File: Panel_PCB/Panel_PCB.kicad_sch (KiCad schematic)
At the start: 87 parts, among them J1 DC, J10 Relay 3, J11 Relay 4, J12 Terminal A, J13 Terminal B, J14 Boton D (4), J2 Bateria, J3 Sensor IN, J4 Sensor OUT, J5 Boton A (1), J6 Boton B (2), J7 Boton C (3), J8 Relay 1, J9 Relay 2, K1 SANYOU_SRD_Form_C, K2 SANYOU_SRD_Form_C, K3 SANYOU_SRD_Form_C, K4 SANYOU_SRD_Form_C, K5 EC2-4.5SNU, K7 SANYOU_SRD_Form_C, Q1 2N2222A, Q2 2N2222A, Q3 2N2222A, Q4 2N2222A, Q7 2N2222A, U1 TLP291, U10 LM1117T-3.3, U12 DS1307+, U13 LM311, U2 TLP291, U3 TLP291, U4 TLP291, U5 LM7805_TO220, U6 LM1117T-3.3, U7 LM7805_TO220, U8 LM7805_TO220, U9 LM1117T-3.3, Y1 Crystal

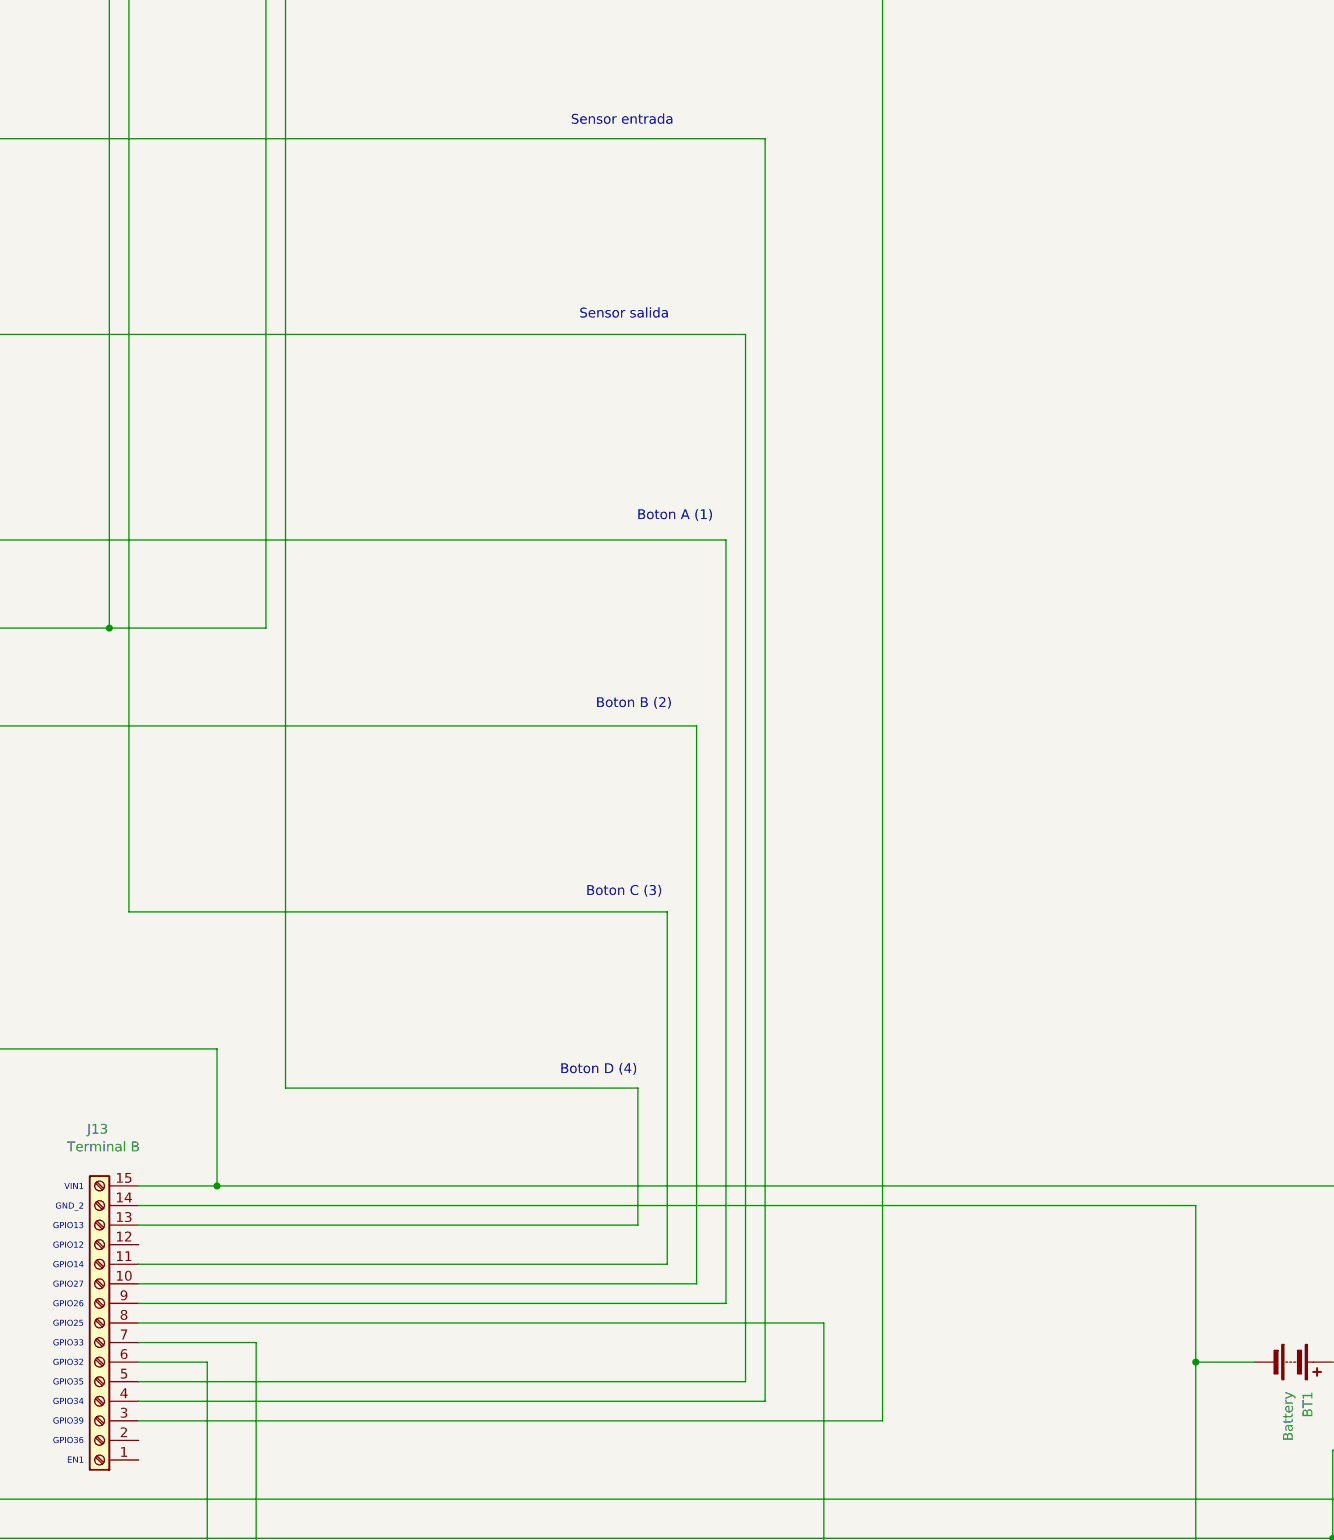
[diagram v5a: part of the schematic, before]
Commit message: Actualización de esquematico: resistencias de pulldown a los pines de los sensores
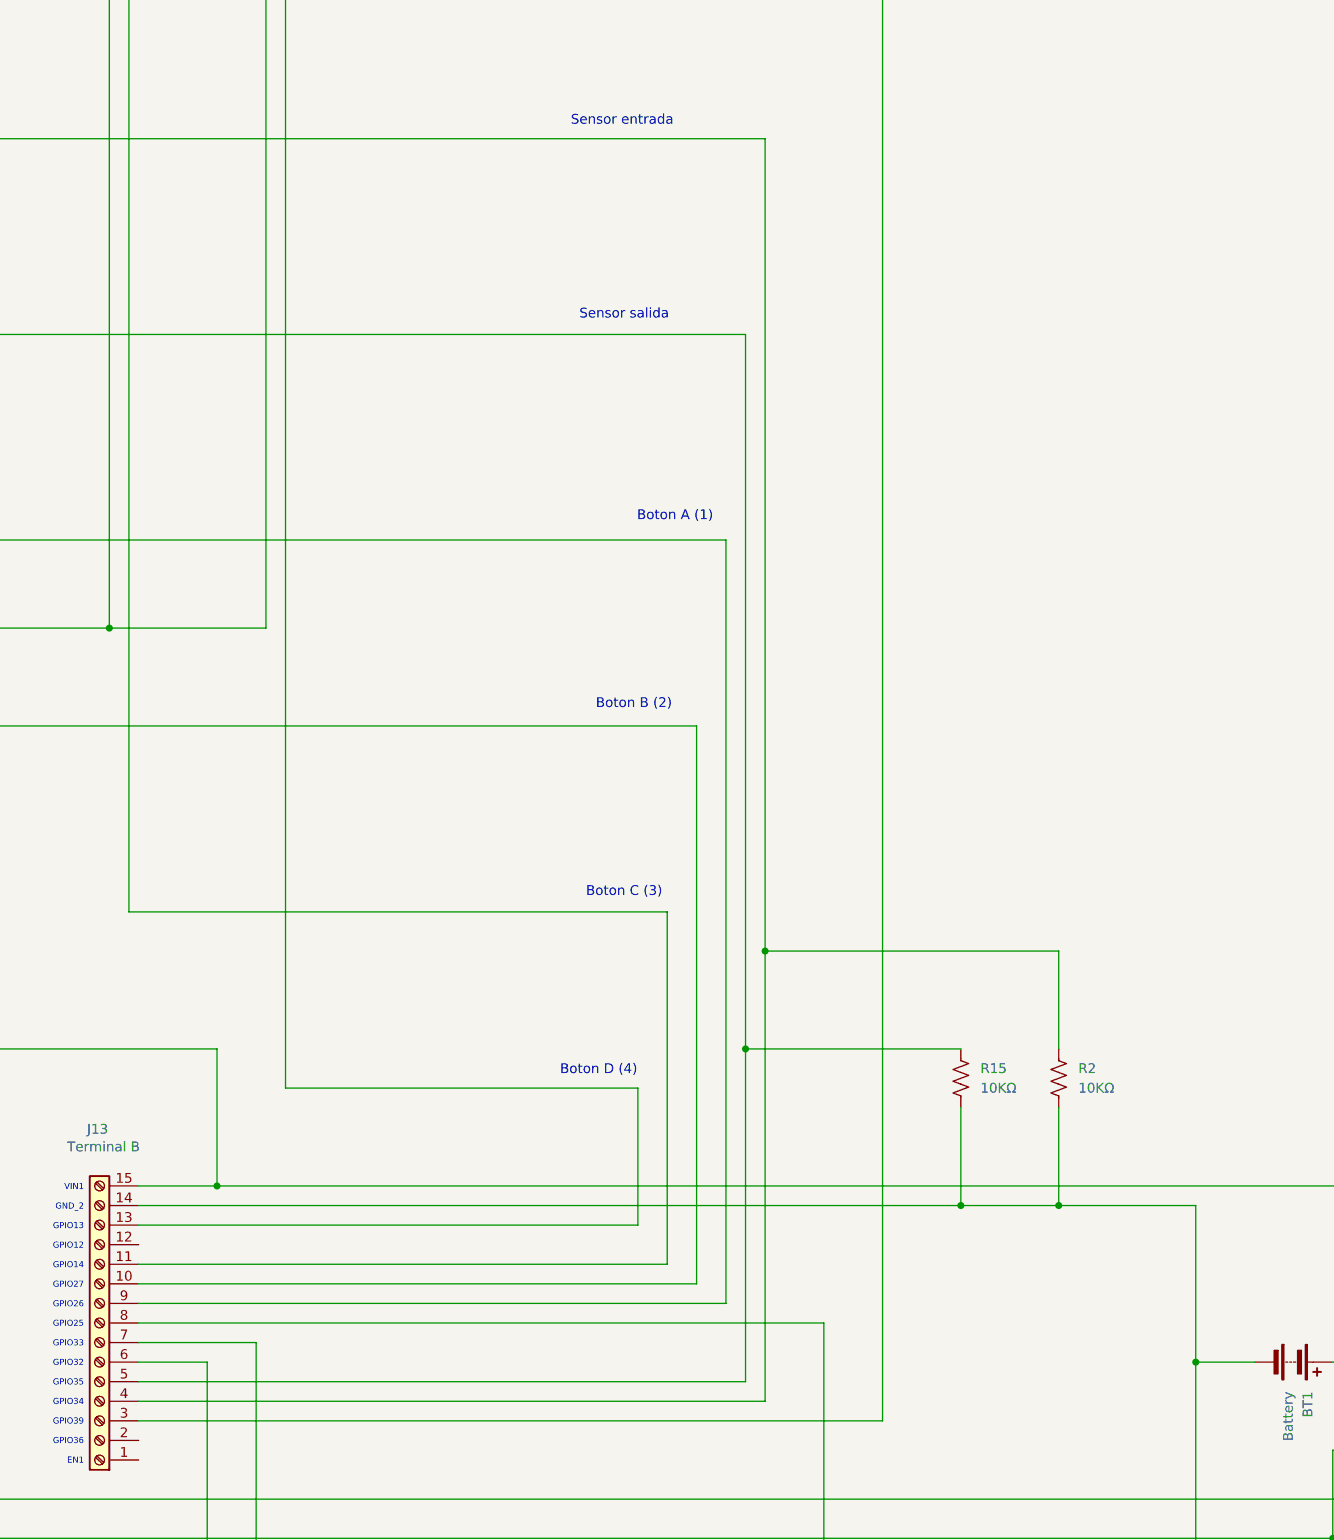
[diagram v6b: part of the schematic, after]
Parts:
- added R15, R2: 10KΩ, Resistor_THT:R_Axial_DIN0207_L6.3mm_D2.5mm_P10.16mm_Horizontal, symbol Device:R_US
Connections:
- net at J13.4 (Pin_4), J3.2 (Pin_2): now also R2.1
- net at J13.5 (Pin_5), J4.2 (Pin_2): now also R15.1
- net at BT1.2 (-), J13.14 (Pin_14), U12.4 (GND): now also R15.2, R2.2

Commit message: Actualización de esquematico
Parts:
- removed D18: 1N4001, Diode_THT:D_DO-41_SOD81_P10.16mm_Horizontal, symbol Diode:1N4001
- removed D2: 12 V, Diode_THT:D_DO-41_SOD81_P10.16mm_Horizontal, symbol Device:D_Zener
- added C4, C5: 25V 4700μF, Capacitor_THT:C_Radial_D18.0mm_H35.5mm_P7.50mm, symbol Device:C_US
- C2: value 35V 4700μF -> 25V 4700μF
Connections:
- net at C10.2, C11.2, C12.2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: now also C4.2, C5.2
- net at C2.1, C7.1, C9.1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: now also C4.1, C5.1
- net at J2.1 (Pin_1), K5.10, K7.3: now also U13.2 (+)
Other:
- note added: "Crear un log de 1 byte para guardar los estados de las salidad (considerar si se necesitan guardar los estados de las entradas)"
- moved on the sheet: C2

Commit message: Información para usar el control remoto
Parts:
- added C6: 25V 4700μF, Capacitor_THT:C_Radial_D18.0mm_H35.5mm_P7.50mm, symbol Device:C_US
- added J15: Control remoto, TerminalBlock:TerminalBlock_Xinya_XY308-2.54-7P_1x07_P2.54mm_Horizontal, symbol Connector:Screw_Terminal_01x07
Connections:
- net at C10.2, C11.2, C12.2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: now also C6.2
- net at C10.1, J12.11 (Pin_11), J12.14 (Pin_14)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: now also C6.1
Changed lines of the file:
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@@
 	)
 	(junction
+		(at 466.09 247.65)
+		(diameter 0)
+		(color 0 0 0 0)
+	)
+	(junction
 		(at 482.6 50.8)
 		(diameter 0)
@@
 	)
 	(junction
+		(at 466.09 267.97)
+		(diameter 0)
+		(color 0 0 0 0)
+	)
+	(junction
 		(at 175.26 106.68)
 		(diameter 0)
@@
 	(wire
 		(pts
-			(xy 435.61 247.65) (xy 542.29 247.65)
+			(xy 435.61 247.65) (xy 466.09 247.65)
 		)
 		(stroke
@@
 	(wire
 		(pts
-			(xy 435.61 267.97) (xy 499.11 267.97)
+			(xy 435.61 267.97) (xy 466.09 267.97)
 		)
 		(stroke
@@
 	(wire
 		(pts
+			(xy 466.09 261.62) (xy 466.09 267.97)
+		)
+		(stroke
+			(width 0)
+			(type default)
+			(color 0 0 0 1)
+		)
+	)
+	(wire
+		(pts
 			(xy 433.07 238.76) (xy 433.07 193.04)
 		)
@@
 	(wire
 		(pts
+			(xy 466.09 267.97) (xy 499.11 267.97)
+		)
+		(stroke
+			(width 0)
+			(type default)
+			(color 0 0 0 1)
+		)
+	)
+	(wire
+		(pts
 			(xy 509.27 107.95) (xy 509.27 205.74)
 		)
@@
 	(wire
 		(pts
+			(xy 466.09 247.65) (xy 466.09 254)
+		)
+		(stroke
+			(width 0)
+			(type default)
+			(color 255 0 0 1)
+		)
+	)
+	(wire
+		(pts
 			(xy 330.2 173.99) (xy 330.2 176.53)
 		)
@@
 	(wire
 		(pts
+			(xy 466.09 247.65) (xy 542.29 247.65)
+		)
+		(stroke
+			(width 0)
+			(type default)
+			(color 255 0 0 1)
+		)
+	)
+	(wire
+		(pts
 			(xy 398.78 339.09) (xy 414.02 339.09)
 		)
@@
 	)
 	(symbol
+		(lib_id "Device:C_US")
+		(at 466.09 257.81 0)
+		(unit 1)
+		(exclude_from_sim no)
+		(in_bom yes)
+		(on_board yes)
+		(dnp no)
+		(fields_autoplaced yes)
+		(property "Reference" "C6"
+			(at 469.9 256.7939 0)
+			(effects
+				(font
+					(size 1.27 1.27)
+				)
+				(justify left)
+			)
+		)
+		(property "Value" "25V  4700μF"
+			(at 469.9 259.3339 0)
+			(effects
+				(font
+					(size 1.27 1.27)
+				)
+				(justify left)
+			)
+		)
+		(property "Footprint" "Capacitor_THT:C_Radial_D18.0mm_H35.5mm_P7.50mm"
+			(at 466.09 257.81 0)
+			(effects
+				(font
+					(size 1.27 1.27)
+				)
+				(hide yes)
+			)
+		)
+		(property "Datasheet" ""
+			(at 466.09 257.81 0)
+			(effects
+				(font
+					(size 1.27 1.27)
+				)
+				(hide yes)
+			)
+		)
+		(property "Description" "capacitor, US symbol"
+			(at 466.09 257.81 0)
+			(effects
+				(font
+					(size 1.27 1.27)
+				)
+				(hide yes)
+			)
+		)
+		(pin "2"
+		)
+		(pin "1"
+		)
+		(instances
+			(project "Panel_PCB"
+				(path "/f7146f60-4eeb-4a38-9050-767b0cc7f13c"
+					(reference "C6")
+					(unit 1)
+				)
+			)
+		)
+	)
+	(symbol
 		(lib_id "Isolator:TLP291")
 		(at 618.49 374.65 270)
@@
 					(unit 1)
 				)
+			)
+		)
+	)
+	(symbol
+		(lib_id "Connector:Screw_Terminal_01x07")
+		(at 519.43 85.09 90)
+		(unit 1)
+		(exclude_from_sim no)
+		(in_bom yes)
+		(on_board yes)
+		(dnp no)
+		(fields_autoplaced yes)
+		(property "Reference" "J15"
+			(at 519.43 78.74 90)
+			(effects
+				(font
+					(size 1.27 1.27)
+				)
+			)
+		)
+		(property "Value" "Control remoto"
+			(at 519.43 81.28 90)
+			(effects
+				(font
+					(size 1.27 1.27)
+				)
+			)
+		)
+		(property "Footprint" "TerminalBlock:TerminalBlock_Xinya_XY308-2.54-7P_1x07_P2.54mm_Horizontal"
+			(at 519.43 85.09 0)
+			(effects
+				(font
+					(size 1.27 1.27)
+				)
+				(hide yes)
+			)
+		)
+		(property "Datasheet" "~"
+			(at 519.43 85.09 0)
+			(effects
+				(font
+					(size 1.27 1.27)
+				)
+				(hide yes)
+			)
+		)
+		(property "Description" "Generic screw terminal, single row, 01x07, script generated (kicad-library-utils/schlib/autogen/connector/)"
+			(at 519.43 85.09 0)
+			(effects
+				(font
+					(size 1.27 1.27)
+				)
+				(hide yes)
+			)
+		)
+		(pin "5"
+		)
+		(pin "2"
+		)
+		(pin "4"
+		)
+		(pin "1"
+		)
+		(pin "3"
+		)
+		(pin "6"
+		)
+		(pin "7"
+		)
+		(instances
+			(project ""
+				(path "/f7146f60-4eeb-4a38-9050-767b0cc7f13c"
+					(reference "J15")
+					(unit 1)
+				)
